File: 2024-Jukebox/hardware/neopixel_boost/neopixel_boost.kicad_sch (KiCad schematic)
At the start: 16 parts, among them J3 Conn_01x03, J4 Conn_01x03, Q1 BSS138, U1 TPS61090

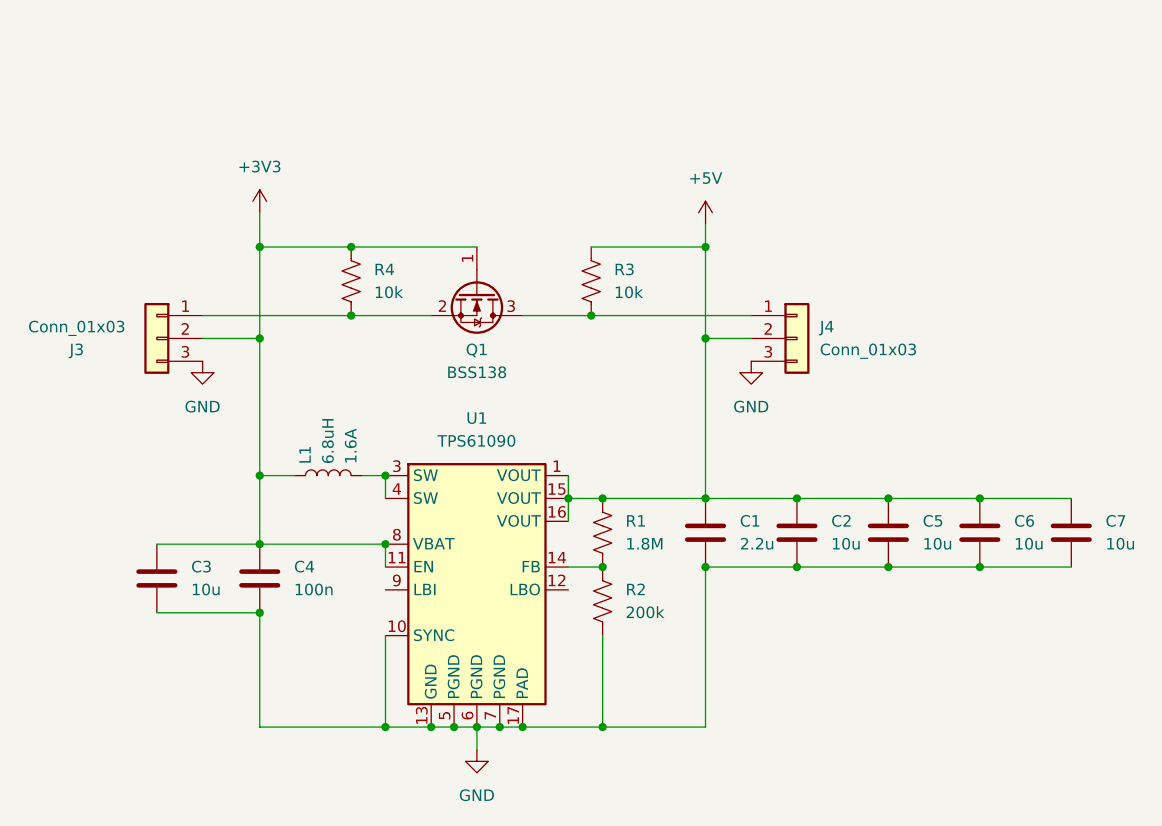
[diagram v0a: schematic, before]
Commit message: Updates to neopixel circuit and ui board firmware
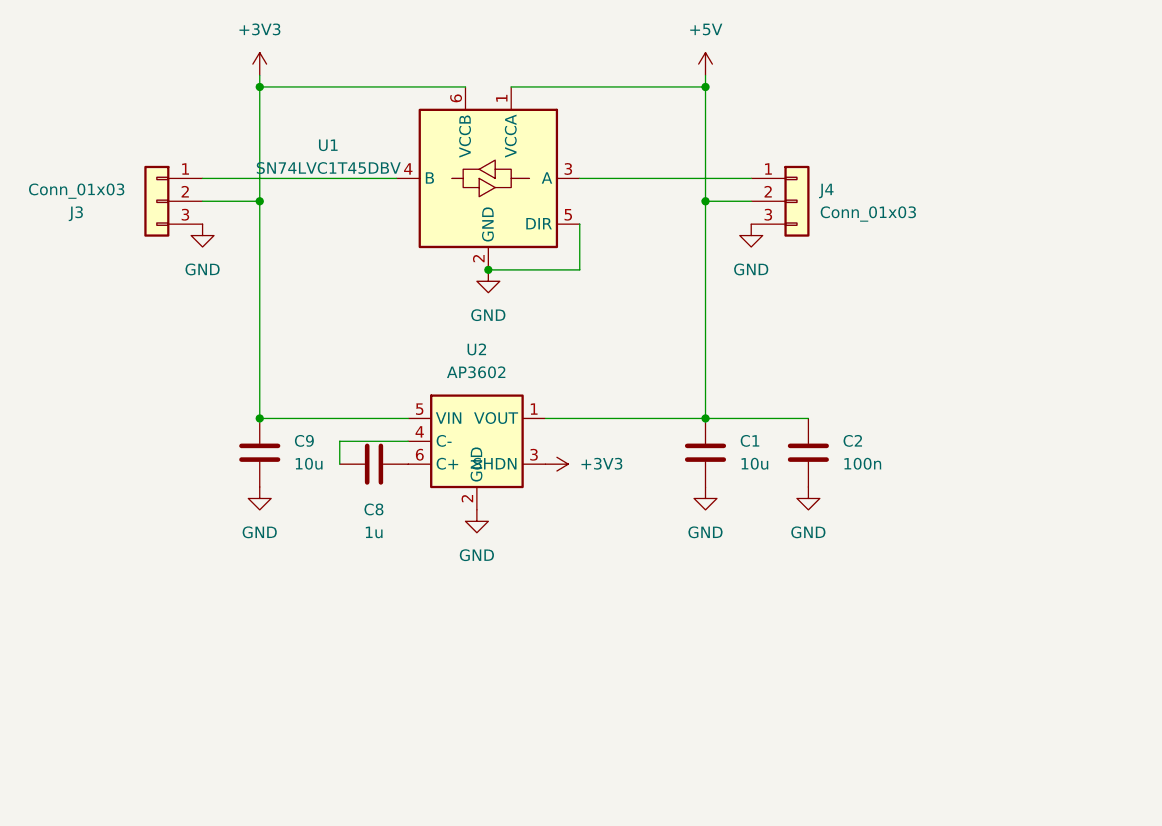
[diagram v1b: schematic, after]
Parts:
- removed C3, C5, C6, C7: 10u, Capacitor_SMD:C_0402_1005Metric, symbol Device:C
- removed C4: 100n, Capacitor_SMD:C_0402_1005Metric, symbol Device:C
- removed L1: 6.8uH_1.0A_4018, Inductor_SMD:L_Taiyo-Yuden_NR-40xx, symbol PCM_4ms_Inductor:6.8uH_1.0A_4018
- removed Q1: BSS138, Package_TO_SOT_SMD:SOT-23, symbol Transistor_FET:BSS138
- removed R1: 1.8M, Resistor_SMD:R_0402_1005Metric, symbol Device:R_US
- removed R2: 200k, Resistor_SMD:R_0402_1005Metric, symbol Device:R_US
- removed R3, R4: 10k, Resistor_SMD:R_0402_1005Metric, symbol Device:R_US
- removed U1: TPS61090, Package_DFN_QFN:Texas_S-PVQFN-N16_EP2.7x2.7mm_ThermalVias, symbol Regulator_Switching:TPS61090
- added C8: 1u, Capacitor_SMD:C_0402_1005Metric, symbol Device:C
- added C9: 10u, Capacitor_SMD:C_0402_1005Metric, symbol Device:C
- added U1: SN74LVC1T45DBV, Package_TO_SOT_SMD:SOT-23-6, symbol Logic_LevelTranslator:SN74LVC1T45DBV
- added U2: AP3602, Package_TO_SOT_SMD:SOT-23-6, symbol Regulator_Switching:MT3608
- C1: value 2.2u -> 10u
- C2: value 10u -> 100n
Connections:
- net +3V3: now also C9.1, U1.6 (VCCB), U2.3 (SHDN), U2.5 (VIN)
- net +5V: now also U1.1 (VCCA), U2.1 (VOUT)
- net GND: now also C9.2, U1.2 (GND), U1.5 (DIR), U2.2 (GND)
- net at J3.1 (Pin_1): now also U1.4 (B)
- net at J4.1 (Pin_1): now also U1.3 (A)
- new net: C8.1, U2.4 (C-)
- new net: C8.2, U2.6 (NC)
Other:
- moved on the sheet: J3, J4
